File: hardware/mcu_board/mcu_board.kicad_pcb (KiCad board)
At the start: 2 copper layers, 57.9 x 100 mm, 20 parts, among them J1 TEMP, J2 LEDS_OUT, J3 LEDS_IN, J4 DISPLAY, J5 RTC, J7 MCU, SW1 RESET, SW2 RotaryEncoder_Switch, U1 ESP32-S3-DevKitC

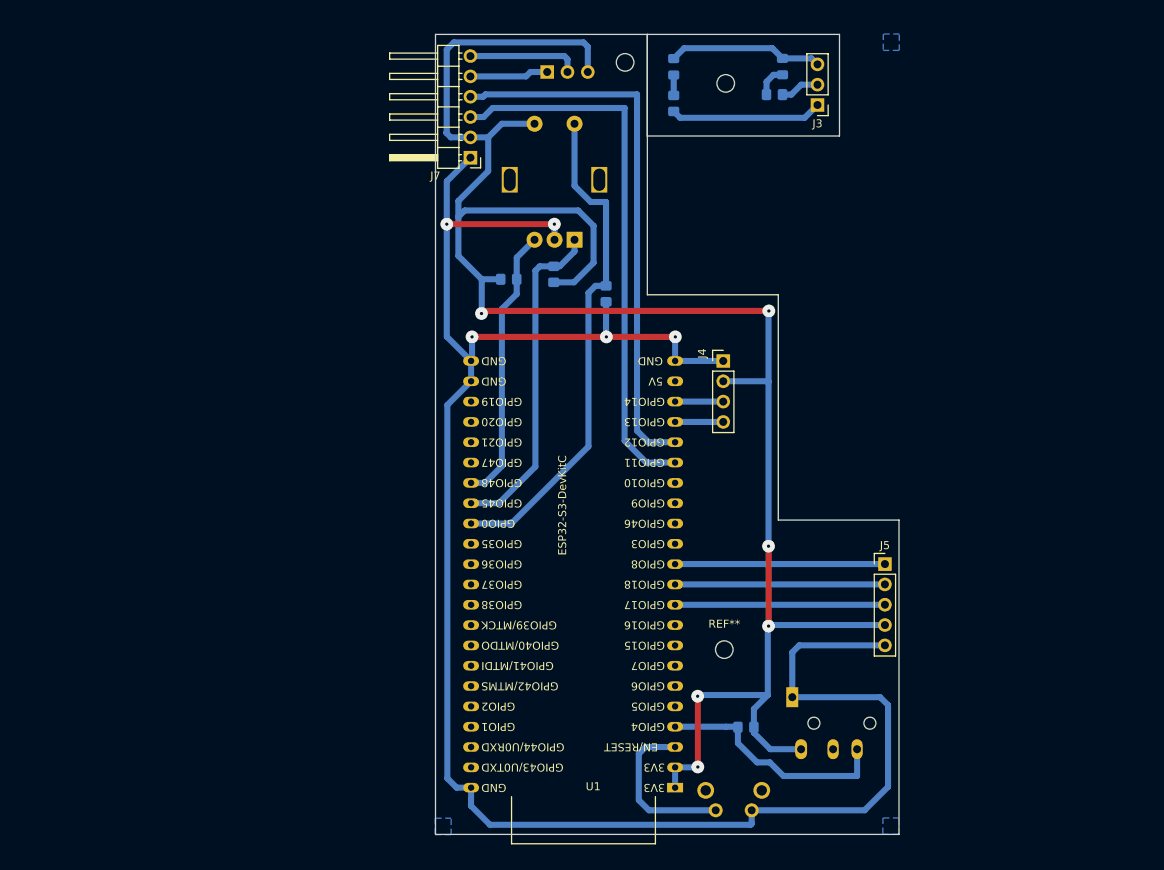
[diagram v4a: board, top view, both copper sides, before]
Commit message: fix boards so they components are on the correct side lol
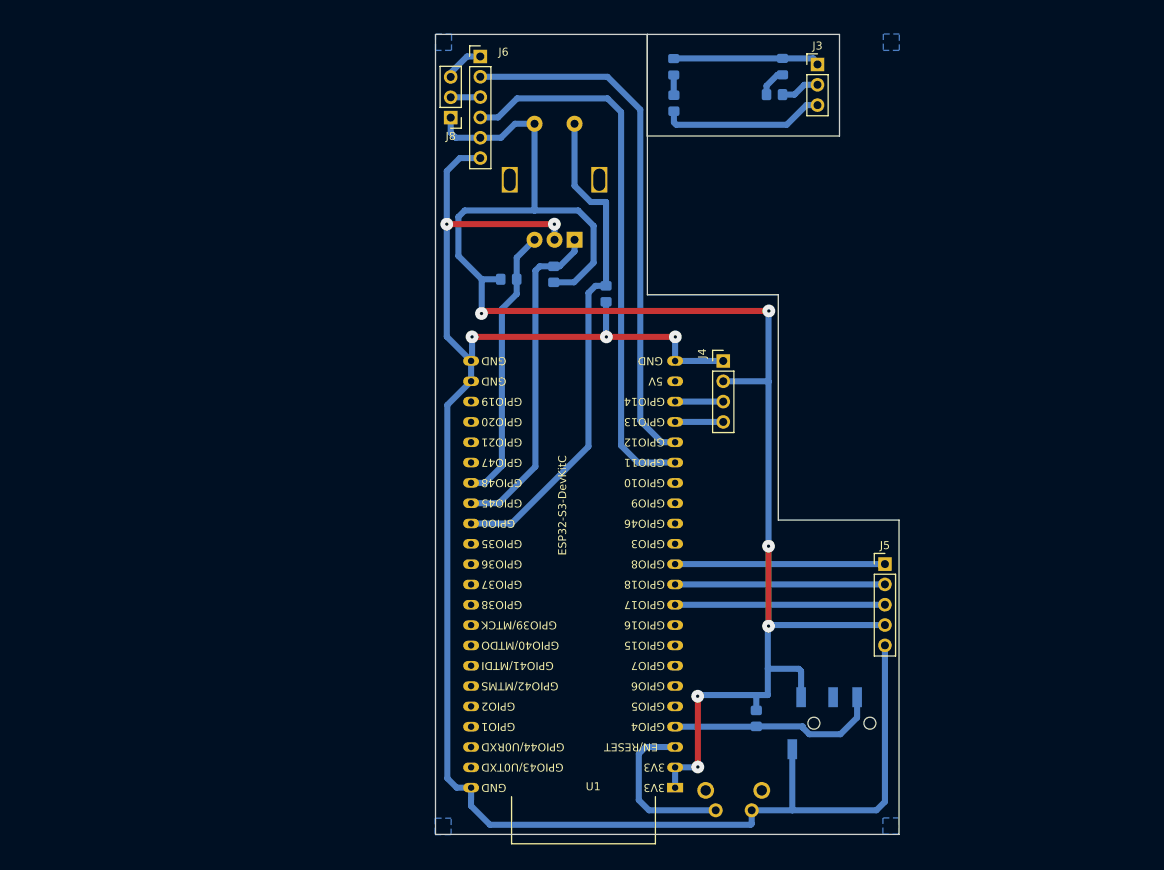
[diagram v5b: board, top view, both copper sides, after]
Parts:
- removed J2: LEDS_OUT, Connector_PinHeader_2.54mm:PinHeader_1x03_P2.54mm_Vertical
- removed J7: MCU, Connector_PinHeader_2.54mm:PinHeader_1x06_P2.54mm_Horizontal
- removed REF** (x3): MountingHole_2.2mm_M2, MountingHole:MountingHole_2.2mm_M2
- added J6: MCU, Connector_PinHeader_2.54mm:PinHeader_1x06_P2.54mm_Vertical, F.Cu at (72.3, 38.8)
- added J8: LEDS_OUT, Connector_PinHeader_2.54mm:PinHeader_1x03_P2.54mm_Vertical, F.Cu at (68.6, 46.4)
- J1: footprint Connector_Audio_2:Jack_3.5mm_PJ320D_Horizontal -> Connector_Audio:Jack_3.5mm_PJ320D_Horizontal
- moved D1 13.6 mm to (110.1, 40.0)
- moved D2 13.6 mm to (96.5, 40.0)
- moved R6 12.6 mm to (109.1, 43.5), turned to 0 degrees
- moved R7 12.6 mm to (96.5, 44.6), turned to -90 degrees
- moved J3 5.07 mm to (114.5, 39.8), turned to 0 degrees
- moved R1 1.70 mm to (106.8, 121.5), turned to 90 degrees
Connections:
- J3 pad 1: Net-(J3-Pin_1) -> Net-(D1-K)
- J3 pad 3: Net-(D1-K) -> Net-(J3-Pin_3)
- R6 pad 2: Net-(J3-Pin_1) -> Net-(J3-Pin_2)
- R7 pad 2: Net-(J3-Pin_2) -> Net-(J3-Pin_3)
- U1 pad 17: RELAY_BOTTOM -> RELAY_BOOST
- U1 pad 18: RELAY_TOP -> RELAY_OFFPEAK
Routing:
- net RELAY_BOTTOM: track 68.8 -> 0.00 mm
- net RELAY_TOP: track 68.8 -> 0.00 mm
- net RELAY_BOOST: track 0.00 -> 68.6 mm
- net RELAY_OFFPEAK: track 0.00 -> 66.1 mm
- net +3.3V: track 239.5 -> 205.7 mm
- net Net-(J3-Pin_3): track 0.00 -> 20.5 mm
- net Net-(J3-Pin_1): track 19.0 -> 0.00 mm
- net LED_TOP: track 13.9 -> 0.00 mm
- net GND: track 240.5 -> 228.4 mm
- net LED_BOTTOM: track 9.82 -> 0.00 mm
- net LED_OFFPEAK: track 0.00 -> 5.06 mm
- net LED_BOOST: track 0.00 -> 3.71 mm
- net WATERTEMP_DATA: track 29.8 -> 26.7 mm
- net Net-(D2-A): track 3.96 -> 2.60 mm
- net Net-(D1-A): track 2.55 -> 3.67 mm
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
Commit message: move screw position
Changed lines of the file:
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@@
     (pcbplotparams
       (layerselection 0x0001000_7ffffffe)
-      (plot_on_all_layers_selection 0x0001000_80000000)
+      (plot_on_all_layers_selection 0x003df30_80000001)
       (disableapertmacros false)
       (usegerberextensions false)
@@
       (dxfimperialunits false)
       (dxfusepcbnewfont true)
-      (psnegative true)
+      (psnegative false)
       (psa4output false)
       (plotreference true)
@@
       (subtractmaskfromsilk false)
       (outputformat 5)
-      (mirror false)
+      (mirror true)
       (drillshape 1)
       (scaleselection 1)
@@
     (fp_line (start 1 0.625) (end 1 -0.625)
       (stroke (width 0.1) (type solid)) (layer "B.Fab"))
-    (pad "1" smd roundrect (at -1 0 270) (size 1.2 1.4) (layers "B.Cu" "B.Paste" "B.Mask") (roundrect_rratio 0.208333)
+    (pad "1" smd roundrect (at -1 0 270) (size 1.2 1.4) (layers "B.Cu" "B.Paste" "B.Mask") (roundrect_rratio 0.2083333333)
       (net 48 "Net-(D2-A)") (pintype "passive"))
-    (pad "2" smd roundrect (at 1 0 270) (size 1.2 1.4) (layers "B.Cu" "B.Paste" "B.Mask") (roundrect_rratio 0.208333)
+    (pad "2" smd roundrect (at 1 0 270) (size 1.2 1.4) (layers "B.Cu" "B.Paste" "B.Mask") (roundrect_rratio 0.2083333333)
       (net 47 "Net-(J3-Pin_3)") (pintype "passive"))
     (model "${KICAD6_3DMODEL_DIR}/Resistor_SMD.3dshapes/R_0805_2012Metric.wrl"
@@
   (segment (start 68.6 41.32) (end 68.6 40.8) (width 0.76) (layer "B.Cu") (net 31))
   (segment (start 68.6 40.8) (end 70.64 38.76) (width 0.76) (layer "B.Cu") (net 31))
-  (segment (start 92.3 45.4) (end 88.2 41.3) (width 0.76) (layer "B.Cu") (net 32))
-  (segment (start 94.97844 86.97844) (end 92.3 84.3) (width 0.76) (layer "B.Cu") (net 32))
-  (segment (start 92.3 84.3) (end 92.3 45.4) (width 0.76) (layer "B.Cu") (net 32))
+  (segment (start 94.97844 86.97844) (end 91.75 83.75) (width 0.76) (layer "B.Cu") (net 32))
+  (segment (start 91.75 83.75) (end 91.75 44.85) (width 0.76) (layer "B.Cu") (net 32))
+  (segment (start 91.75 44.85) (end 88.2 41.3) (width 0.76) (layer "B.Cu") (net 32))
+  (segment (start 88.2 41.3) (end 72.3 41.3) (width 0.76) (layer "B.Cu") (net 32))
   (segment (start 96.650001 86.97844) (end 94.97844 86.97844) (width 0.76) (layer "B.Cu") (net 32))
-  (segment (start 88.2 41.3) (end 72.3 41.3) (width 0.76) (layer "B.Cu") (net 32))
   (segment (start 108.0775 43.525) (end 108.0775 42.4225) (width 0.76) (layer "B.Cu") (net 33))
   (segment (start 109.45 41.05) (end 110.0775 41.05) (width 0.76) (layer "B.Cu") (net 33))

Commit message: minor tweaks
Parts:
- moved J5 21.2 mm to (101.7, 102.2)
- moved D1 4.50 mm to (114.6, 40.0)
- moved D2 4.50 mm to (101.0, 40.0)
- moved J3 4.50 mm to (119.0, 39.8)
- moved R6 4.50 mm to (113.6, 43.5)
- moved R7 4.50 mm to (101.0, 44.6)
- moved SW1 3.78 mm to (105.5, 133.2)
- moved R5 2.08 mm to (88.8, 66.5), turned to 180 degrees
- moved J8 1.70 mm to (66.9, 46.4)
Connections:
- U1 pad 16: unconnected-(U1-GPIO10/ADC1_CH9-Pad16) -> ROT_SW
- U1 pad 31: ROT_SW -> unconnected-(U1-GPIO0-Pad31)
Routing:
- net +3.3V: track 205.7 -> 262.1 mm, vias 6 -> 4
- net RTC_SDA: track 26.2 -> 4.15 mm
- net RTC_SQW: track 26.2 -> 4.15 mm
- net RTC_SCK: track 26.2 -> 4.17 mm
- net ROT_SW: track 63.5 -> 55.0 mm
- net GND: track 228.4 -> 234.0 mm
- net RESET: track 20.8 -> 16.0 mm
- net LED_BOOST: track 3.71 -> 5.42 mm
- net LED_OFFPEAK: track 5.06 -> 6.45 mm
- net RELAY_OFFPEAK: track 66.1 -> 67.2 mm
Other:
- board size 57.9 x 100 mm -> 60.3 x 100 mm

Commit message: v3 first draft
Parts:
- D1: value LED -> LED_BT
- D2: value LED -> LED_OP
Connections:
- U1 pad 15: unconnected-(U1-GPIO9/ADC1_CH8-Pad15) -> ROT_SW
- U1 pad 16: ROT_SW -> unconnected-(U1-GPIO10/ADC1_CH9-Pad16)
- U1 pad 27: unconnected-(U1-GPIO21-Pad27) -> ROT_DT
- U1 pad 28: unconnected-(U1-GPIO47-Pad28) -> ROT_CLK
- U1 pad 29: ROT_DT -> unconnected-(U1-GPIO48-Pad29)
- U1 pad 30: ROT_CLK -> unconnected-(U1-GPIO45-Pad30)
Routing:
- net ROT_DT: track 34.7 -> 30.2 mm
- net ROT_CLK: track 41.8 -> 37.5 mm
- net ROT_SW: track 55.0 -> 57.8 mm
- net GND: track 234.0 -> 236.4 mm
